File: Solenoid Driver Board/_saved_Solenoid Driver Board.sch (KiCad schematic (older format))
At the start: 25 parts, among them J1 CH1, J2 Solenoid, J3 RGB_LED, J4 DEBUG, J5 MAIN, J6 CH2, J7 CH3, J8 MAIN, Q1 IRLB8721PBF, U1 AMS1117-5.0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

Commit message: Moved fade to TIM4, started work on new board revision
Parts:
- R5, R6, R7, R8: footprint Resistors_SMD:R_0805_HandSoldering -> Resistors_SMD:R_1206_HandSoldering
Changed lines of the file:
@@
 $EndComp
 $Comp
-L +12V #PWR1
+L +12V #PWR01
 U 1 1 58F576B7
 P 2100 1400
-F 0 "#PWR1" H 2100 1250 50  0001 C CNN
+F 0 "#PWR01" H 2100 1250 50  0001 C CNN
 F 1 "+12V" H 2100 1540 50  0000 C CNN
 F 2 "" H 2100 1400 50  0001 C CNN
@@
 $EndComp
 $Comp
-L +5V #PWR4
+L +5V #PWR02
 U 1 1 58F576D3
 P 3100 1400
-F 0 "#PWR4" H 3100 1250 50  0001 C CNN
+F 0 "#PWR02" H 3100 1250 50  0001 C CNN
 F 1 "+5V" H 3100 1540 50  0000 C CNN
 F 2 "" H 3100 1400 50  0001 C CNN
@@
 $EndComp
 $Comp
-L GND #PWR3
+L GND #PWR03
 U 1 1 58F576F3
 P 2600 1850
-F 0 "#PWR3" H 2600 1600 50  0001 C CNN
+F 0 "#PWR03" H 2600 1600 50  0001 C CNN
 F 1 "GND" H 2600 1700 50  0000 C CNN
 F 2 "" H 2600 1850 50  0001 C CNN
@@
 	2900 1400 3500 1400
 $Comp
-L +5V #PWR6
+L +5V #PWR04
 U 1 1 58F5771C
 P 5200 1600
-F 0 "#PWR6" H 5200 1450 50  0001 C CNN
+F 0 "#PWR04" H 5200 1450 50  0001 C CNN
 F 1 "+5V" H 5200 1740 50  0000 C CNN
 F 2 "" H 5200 1600 50  0001 C CNN
@@
 $EndComp
 $Comp
-L GND #PWR7
+L GND #PWR05
 U 1 1 58F57736
 P 5200 3650
-F 0 "#PWR7" H 5200 3400 50  0001 C CNN
+F 0 "#PWR05" H 5200 3400 50  0001 C CNN
 F 1 "GND" H 5200 3500 50  0000 C CNN
 F 2 "" H 5200 3650 50  0001 C CNN
@@
 SWIM
 $Comp
-L GND #PWR23
+L GND #PWR06
 U 1 1 58F57AF4
 P 9950 1300
-F 0 "#PWR23" H 9950 1050 50  0001 C CNN
+F 0 "#PWR06" H 9950 1050 50  0001 C CNN
 F 1 "GND" H 9950 1150 50  0000 C CNN
 F 2 "" H 9950 1300 50  0001 C CNN
@@
 $EndComp
 $Comp
-L +5V #PWR22
+L +5V #PWR07
 U 1 1 58F57B17
 P 9950 1100
-F 0 "#PWR22" H 9950 950 50  0001 C CNN
+F 0 "#PWR07" H 9950 950 50  0001 C CNN
 F 1 "+5V" H 9950 1240 50  0000 C CNN
 F 2 "" H 9950 1100 50  0001 C CNN
@@
 $EndComp
 $Comp
-L GND #PWR19
+L GND #PWR08
 U 1 1 58F58125
 P 8750 4250
-F 0 "#PWR19" H 8750 4000 50  0001 C CNN
+F 0 "#PWR08" H 8750 4000 50  0001 C CNN
 F 1 "GND" H 8750 4100 50  0000 C CNN
 F 2 "" H 8750 4250 50  0001 C CNN
@@
 $EndComp
 $Comp
-L +12V #PWR18
+L +12V #PWR09
 U 1 1 58F5833A
 P 8750 3150
-F 0 "#PWR18" H 8750 3000 50  0001 C CNN
+F 0 "#PWR09" H 8750 3000 50  0001 C CNN
 F 1 "+12V" H 8750 3290 50  0000 C CNN
 F 2 "" H 8750 3150 50  0001 C CNN
@@
 $EndComp
 $Comp
-L +12V #PWR20
+L +12V #PWR010
 U 1 1 58F586EE
 P 9900 2050
-F 0 "#PWR20" H 9900 1900 50  0001 C CNN
+F 0 "#PWR010" H 9900 1900 50  0001 C CNN
 F 1 "+12V" H 9900 2190 50  0000 C CNN
 F 2 "" H 9900 2050 50  0001 C CNN
@@
 $EndComp
 $Comp
-L GND #PWR21
+L GND #PWR011
 U 1 1 58F58726
 P 9900 2150
-F 0 "#PWR21" H 9900 1900 50  0001 C CNN
+F 0 "#PWR011" H 9900 1900 50  0001 C CNN
 F 1 "GND" H 9900 2000 50  0000 C CNN
 F 2 "" H 9900 2150 50  0001 C CNN
@@
 $EndComp
 $Comp
-L +5V #PWR2
+L +5V #PWR012
 U 1 1 58FB95C2
 P 2350 2400
-F 0 "#PWR2" H 2350 2250 50  0001 C CNN
+F 0 "#PWR012" H 2350 2250 50  0001 C CNN
 F 1 "+5V" H 2350 2540 50  0000 C CNN
 F 2 "" H 2350 2400 50  0001 C CNN
@@
 Connection ~ 2100 1400
 $Comp
-L GND #PWR5
+L GND #PWR013
 U 1 1 58FBA70F
 P 3100 1850
-F 0 "#PWR5" H 3100 1600 50  0001 C CNN
+F 0 "#PWR013" H 3100 1600 50  0001 C CNN
 F 1 "GND" H 3100 1700 50  0000 C CNN
 F 2 "" H 3100 1850 50  0001 C CNN
@@
 	6500 3200 6850 3200
 $Comp
-L +5V #PWR8
+L +5V #PWR014
 U 1 1 5904B931
 P 6850 3300
-F 0 "#PWR8" H 6850 3150 50  0001 C CNN
+F 0 "#PWR014" H 6850 3150 50  0001 C CNN
 F 1 "+5V" H 6850 3440 50  0000 C CNN
 F 2 "" H 6850 3300 50  0001 C CNN
@@
 $EndComp
 $Comp
-L GND #PWR9
+L GND #PWR015
 U 1 1 5904B984
 P 6850 3400
-F 0 "#PWR9" H 6850 3150 50  0001 C CNN
+F 0 "#PWR015" H 6850 3150 50  0001 C CNN
 F 1 "GND" H 6850 3250 50  0000 C CNN
 F 2 "" H 6850 3400 50  0001 C CNN
@@
 F 0 "R7" V 1880 1550 50  0000 C CNN
 F 1 "10k" V 1800 1550 50  0000 C CNN
-F 2 "Resistors_SMD:R_0805_HandSoldering" V 1730 1550 50  0001 C CNN
+F 2 "Resistors_SMD:R_1206_HandSoldering" V 1730 1550 50  0001 C CNN
 F 3 "" H 1800 1550 50  0001 C CNN
 	1    1800 1550
@@
 F 0 "R6" V 1730 1550 50  0000 C CNN
 F 1 "10k" V 1650 1550 50  0000 C CNN
-F 2 "Resistors_SMD:R_0805_HandSoldering" V 1580 1550 50  0001 C CNN
+F 2 "Resistors_SMD:R_1206_HandSoldering" V 1580 1550 50  0001 C CNN
 F 3 "" H 1650 1550 50  0001 C CNN
 	1    1650 1550
@@
 F 0 "R5" V 1580 1550 50  0000 C CNN
 F 1 "10k" V 1500 1550 50  0000 C CNN
-F 2 "Resistors_SMD:R_0805_HandSoldering" V 1430 1550 50  0001 C CNN
+F 2 "Resistors_SMD:R_1206_HandSoldering" V 1430 1550 50  0001 C CNN
 F 3 "" H 1500 1550 50  0001 C CNN
 	1    1500 1550
@@
 F 0 "R8" V 2330 2100 50  0000 C CNN
 F 1 "10k" V 2250 2100 50  0000 C CNN
-F 2 "Resistors_SMD:R_0805_HandSoldering" V 2180 2100 50  0001 C CNN
+F 2 "Resistors_SMD:R_1206_HandSoldering" V 2180 2100 50  0001 C CNN
 F 3 "" H 2250 2100 50  0001 C CNN
 	1    2250 2100
@@
 $EndComp
 $Comp
-L +12V #PWR16
+L +12V #PWR016
 U 1 1 594F0627
 P 8600 2100
-F 0 "#PWR16" H 8600 1950 50  0001 C CNN
+F 0 "#PWR016" H 8600 1950 50  0001 C CNN
 F 1 "+12V" H 8600 2240 50  0000 C CNN
 F 2 "" H 8600 2100 50  0001 C CNN
@@
 $EndComp
 $Comp
-L GND #PWR17
+L GND #PWR017
 U 1 1 594F062D
 P 8600 2200
-F 0 "#PWR17" H 8600 1950 50  0001 C CNN
+F 0 "#PWR017" H 8600 1950 50  0001 C CNN
 F 1 "GND" H 8600 2050 50  0000 C CNN
 F 2 "" H 8600 2200 50  0001 C CNN
@@
 $EndComp
 $Comp
-L GND #PWR11
+L GND #PWR018
 U 1 1 594F0877
 P 7000 1300
-F 0 "#PWR11" H 7000 1050 50  0001 C CNN
+F 0 "#PWR018" H 7000 1050 50  0001 C CNN
 F 1 "GND" H 7000 1150 50  0000 C CNN
 F 2 "" H 7000 1300 50  0001 C CNN
@@
 	7050 1100 7100 1100
 $Comp
-L +5V #PWR10
+L +5V #PWR019
 U 1 1 594F0C76
 P 7000 1200
-F 0 "#PWR10" H 7000 1050 50  0001 C CNN
+F 0 "#PWR019" H 7000 1050 50  0001 C CNN
 F 1 "+5V" H 7000 1340 50  0000 C CNN
 F 2 "" H 7000 1200 50  0001 C CNN
@@
 $EndComp
 $Comp
-L GND #PWR13
+L GND #PWR020
 U 1 1 594F0D4C
 P 7800 1300
-F 0 "#PWR13" H 7800 1050 50  0001 C CNN
+F 0 "#PWR020" H 7800 1050 50  0001 C CNN
 F 1 "GND" H 7800 1150 50  0000 C CNN
 F 2 "" H 7800 1300 50  0001 C CNN
@@
 	7850 1100 7900 1100
 $Comp
-L +5V #PWR12
+L +5V #PWR021
 U 1 1 594F0D57
 P 7800 1200
-F 0 "#PWR12" H 7800 1050 50  0001 C CNN
+F 0 "#PWR021" H 7800 1050 50  0001 C CNN
 F 1 "+5V" H 7800 1340 50  0000 C CNN
 F 2 "" H 7800 1200 50  0001 C CNN
@@
 $EndComp
 $Comp
-L GND #PWR15
+L GND #PWR022
 U 1 1 594F0E91
 P 8550 1300
-F 0 "#PWR15" H 8550 1050 50  0001 C CNN
+F 0 "#PWR022" H 8550 1050 50  0001 C CNN
 F 1 "GND" H 8550 1150 50  0000 C CNN
 F 2 "" H 8550 1300 50  0001 C CNN
@@
 	8600 1100 8650 1100
 $Comp
-L +5V #PWR14
+L +5V #PWR023
 U 1 1 594F0E9C
 P 8550 1200
-F 0 "#PWR14" H 8550 1050 50  0001 C CNN
+F 0 "#PWR023" H 8550 1050 50  0001 C CNN
 F 1 "+5V" H 8550 1340 50  0000 C CNN
 F 2 "" H 8550 1200 50  0001 C CNN

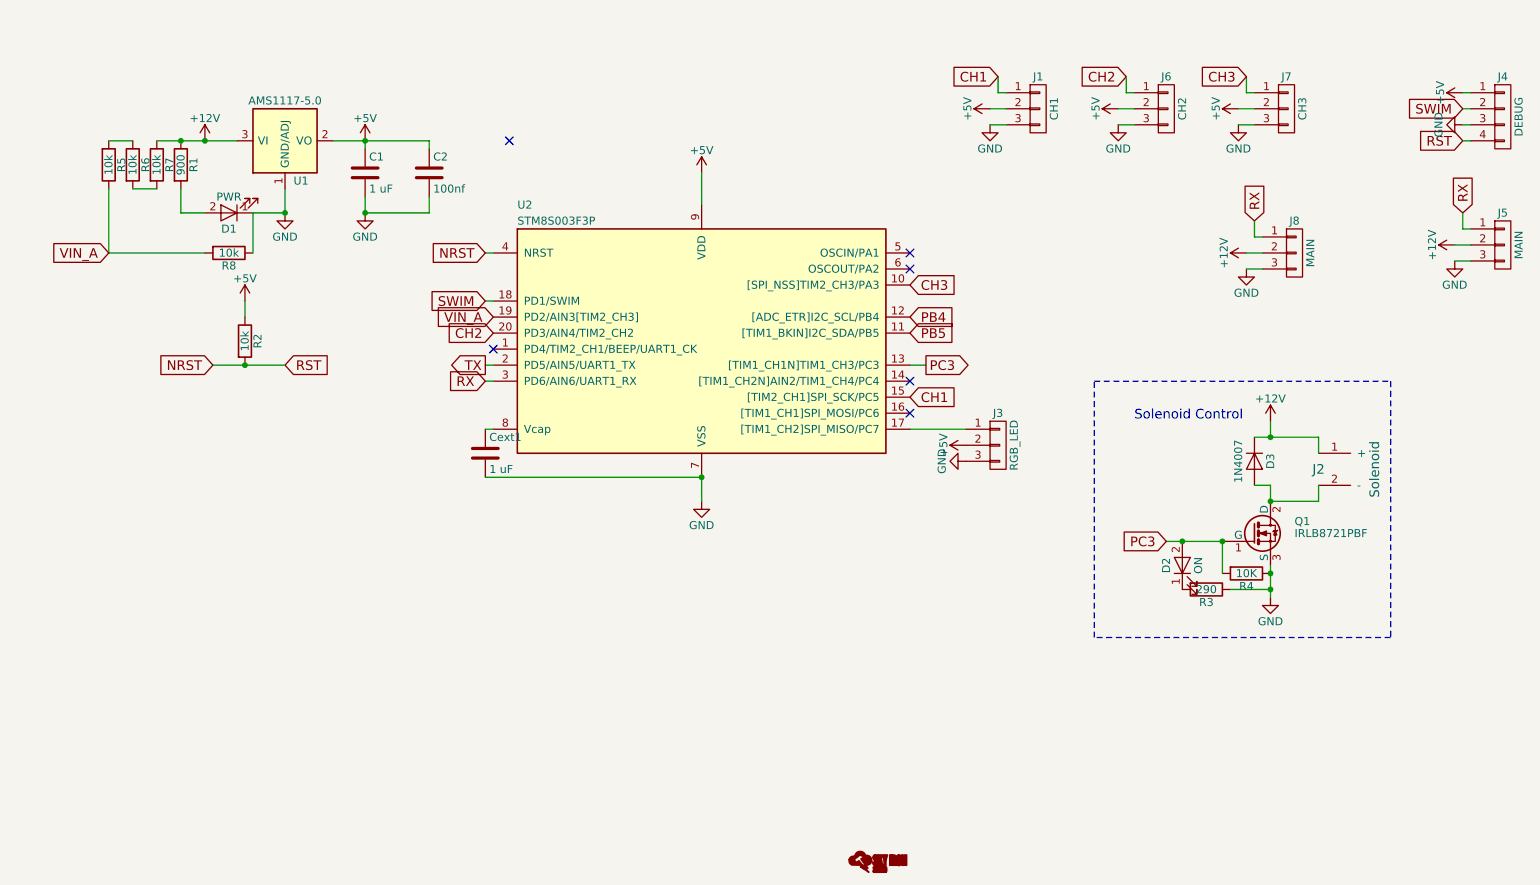
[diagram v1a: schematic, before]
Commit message: Added IWDG timer support
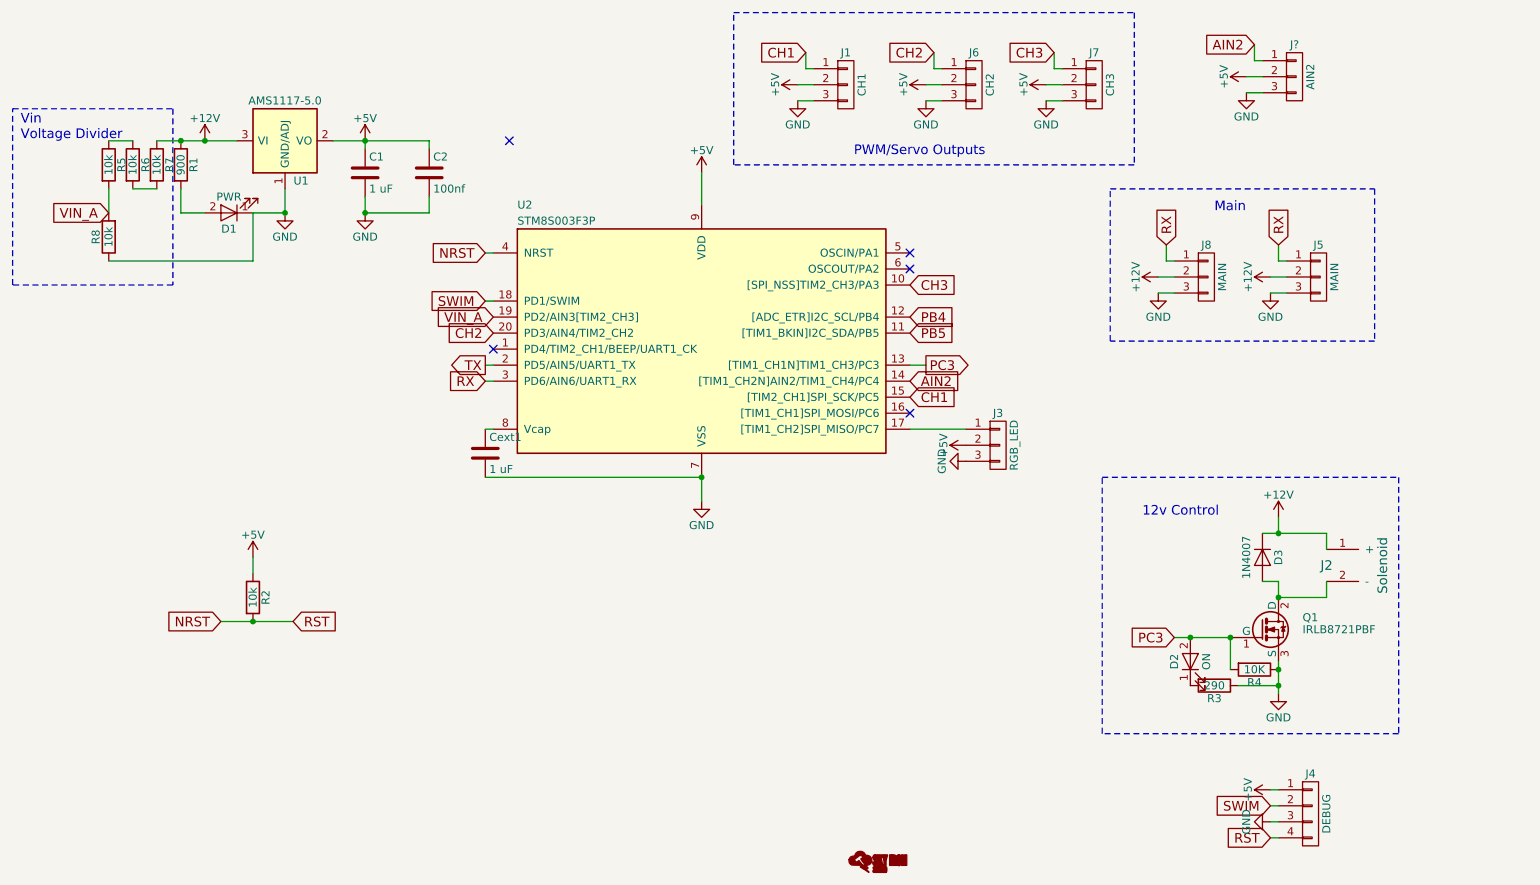
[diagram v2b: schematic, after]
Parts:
- added J?: AIN2, Pin_Headers:Pin_Header_Straight_1x03_Pitch2.54mm, symbol CONN_01X03
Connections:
- net +5V: now also J?.2 (P2)
- net GND: now also J?.3 (P3)
- net VIN_A: now also R5.2; no longer R5.1
- net AIN2: now reaches U2.14 ([TIM1_CH2N]AIN2/TIM1_CH4/PC4)
- net AIN2: now also J?.1 (P1)
- net at R6.1: now also R5.1; no longer R5.2
- no-connect marks 6 -> 5
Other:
- note added: "12v Control"
- note added: "Main"
- note added: "PWM/Servo Outputs"
- note added: "Vin \nVoltage Divider"
- note removed: "Solenoid Control"
- moved on the sheet: D2, D3, J1, J2, J4, J5, J6, J7, J8, Q1, R2, R3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
